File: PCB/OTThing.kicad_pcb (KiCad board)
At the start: 2 copper layers, 51.5 x 76.5 mm, 60 parts, among them IC1 TPS61041, J3 USB_C_Receptacle_USB2.0, Q1 BC858, Q2 BC847, Q3 BC847, Q4 BC858, Q5 BC858, Q6 BC847, Q7 BC858, SW1 RST/CONFIG, U1 ESP32-WROOM-32, U3 LTV-356T, U4 LTV-356T, U5 CH340C, U6 AMS1117-3.3

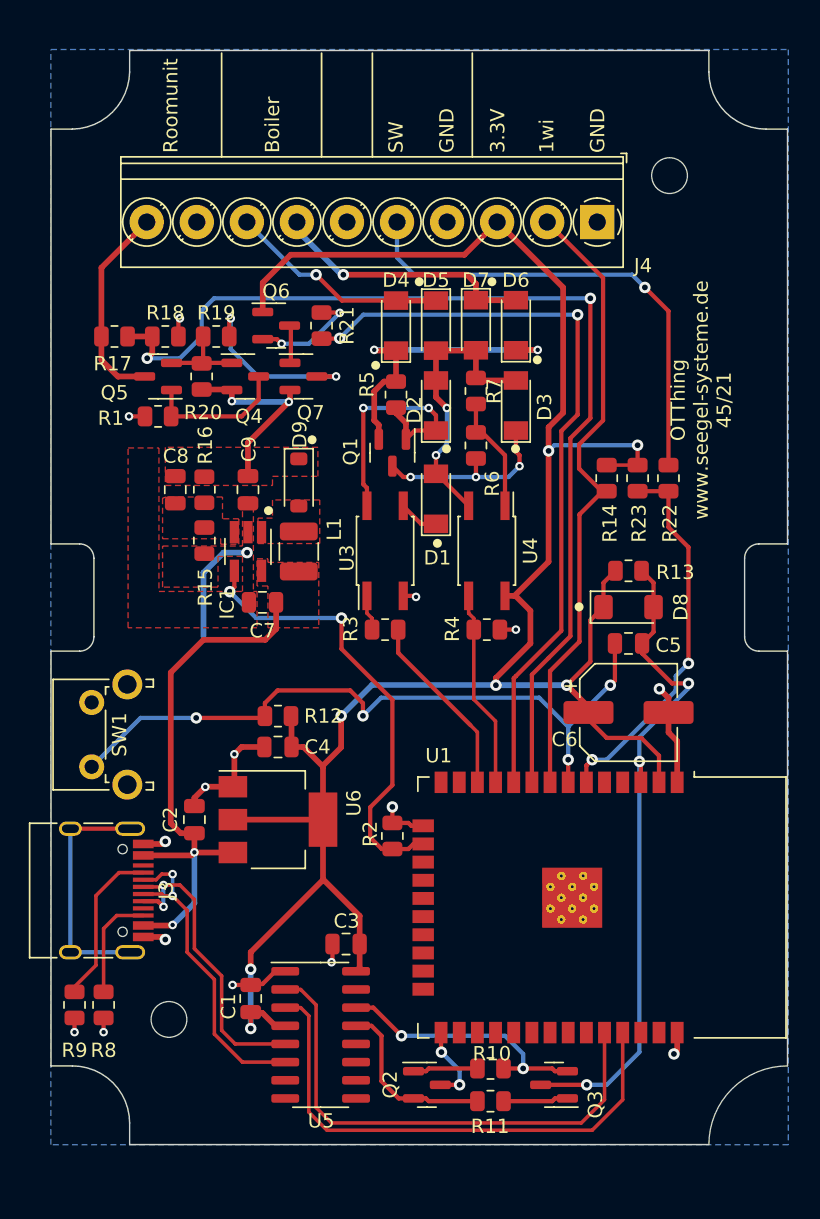
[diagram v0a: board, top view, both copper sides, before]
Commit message: change MCU redesign OT interfaces
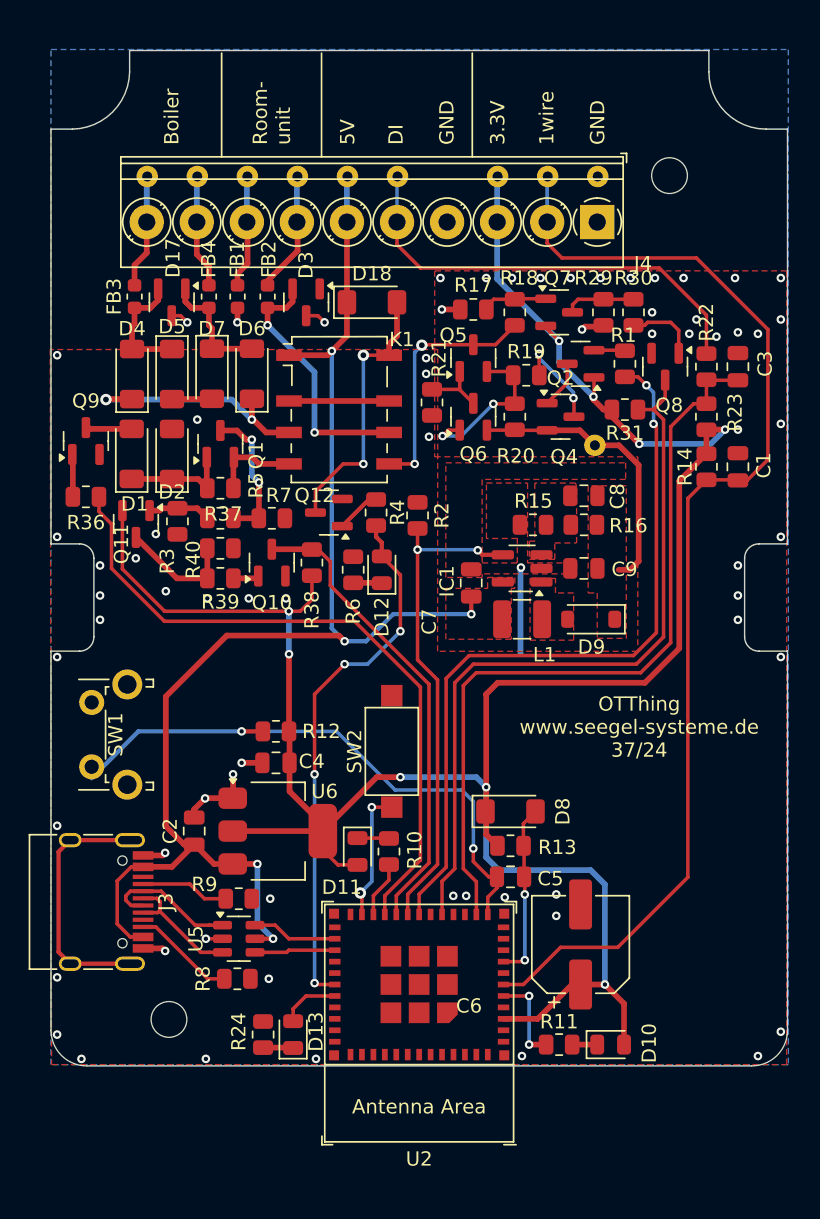
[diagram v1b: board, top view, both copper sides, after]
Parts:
- removed Q3: BC847, Package_TO_SOT_SMD:SOT-23
- removed U1: ESP32-WROOM-32, RF_Module:ESP32-WROOM-32
- removed U3, U4: LTV-356T, Package_SO:SO-4_4.4x3.6mm_P2.54mm
- added D10: RD, LED_SMD:LED_0805_2012Metric, F.Cu at (154.4, 143.9)
- added D11: GN, LED_SMD:LED_0805_2012Metric, F.Cu at (136.7, 130.4)
- added D12: YL, LED_SMD:LED_0805_2012Metric, F.Cu at (138.4, 110.7)
- added D13: GN, LED_SMD:LED_0805_2012Metric, F.Cu at (132.2, 143.2)
- added D17: D_Zener_Dual_CommonAnode_KKA_Parallel, Package_TO_SOT_SMD:SOT-23, F.Cu at (123.7, 92.0)
- added D18: LL4148, Diode_SMD:D_MiniMELF, F.Cu at (137.7, 92.0)
- added FB1: FerriteBead_Small, Inductor_SMD:L_0603_1608Metric, F.Cu at (128.3, 91.6)
- added FB2: FerriteBead_Small, Inductor_SMD:L_0603_1608Metric, F.Cu at (130.4, 91.6)
- added FB3: FerriteBead_Small, Inductor_SMD:L_0603_1608Metric, F.Cu at (121.1, 91.6)
- added FB4: FerriteBead_Small, Inductor_SMD:L_0603_1608Metric, F.Cu at (126.3, 91.6)
- added K1: G6K-2, Relay_SMD:Relay_DPDT_Omron_G6K-2F-Y, F.Cu at (135.4, 99.5)
- added Q10: BC847C, Package_TO_SOT_SMD:SOT-23, F.Cu at (130.7, 110.2)
- added Q11: BC857C, Package_TO_SOT_SMD:SOT-23, F.Cu at (121.2, 107.5)
- added Q12: BC847C, Package_TO_SOT_SMD:SOT-23, F.Cu at (134.7, 106.7)
- added Q8: BC847C, Package_TO_SOT_SMD:SOT-23, F.Cu at (158.2, 96.5)
- added Q9: BC847C, Package_TO_SOT_SMD:SOT-23, F.Cu at (117.7, 101.7)
- added R24: 100, Resistor_SMD:R_0805_2012Metric, F.Cu at (130.1, 143.2)
- added R29: 4k7, Resistor_SMD:R_0805_2012Metric, F.Cu at (153.9, 92.7)
- added R30: 4k7, Resistor_SMD:R_0805_2012Metric, F.Cu at (156.0, 92.7)
- added R31: 4k7, Resistor_SMD:R_0805_2012Metric, F.Cu at (155.4, 99.5)
- added R36: 4k7, Resistor_SMD:R_0805_2012Metric, F.Cu at (117.7, 105.6)
- added R37: 10k, Resistor_SMD:R_0805_2012Metric, F.Cu at (127.1, 107.1)
- added R38: 4k7, Resistor_SMD:R_0805_2012Metric, F.Cu at (133.5, 110.2)
- added R39: 4k7, Resistor_SMD:R_0805_2012Metric, F.Cu at (127.1, 111.3)
- added R40: 4k7, Resistor_SMD:R_0805_2012Metric, F.Cu at (127.1, 109.2)
- added SW2: BOOT, Button_Switch_SMD:SW_SPST_CK_RS282G05A3, F.Cu at (139.1, 123.4)
- added TP1: ~, TestPoint:TestPoint_THTPad_D1.5mm_Drill0.7mm, B.Cu at (153.5, 83.2)
- added TP10: ~, TestPoint:TestPoint_THTPad_D1.5mm_Drill0.7mm, B.Cu at (153.3, 102.0)
- added TP2: ~, TestPoint:TestPoint_THTPad_D1.5mm_Drill0.7mm, B.Cu at (150.0, 83.2)
- added TP3: ~, TestPoint:TestPoint_THTPad_D1.5mm_Drill0.7mm, B.Cu at (146.5, 83.2)
- added TP4: ~, TestPoint:TestPoint_THTPad_D1.5mm_Drill0.7mm, B.Cu at (139.5, 83.2)
- added TP5: ~, TestPoint:TestPoint_THTPad_D1.5mm_Drill0.7mm, B.Cu at (136.0, 83.2)
- added TP6: ~, TestPoint:TestPoint_THTPad_D1.5mm_Drill0.7mm, B.Cu at (132.5, 83.2)
- added TP7: ~, TestPoint:TestPoint_THTPad_D1.5mm_Drill0.7mm, B.Cu at (129.0, 83.2)
- added TP8: ~, TestPoint:TestPoint_THTPad_D1.5mm_Drill0.7mm, B.Cu at (125.5, 83.2)
- added TP9: ~, TestPoint:TestPoint_THTPad_D1.5mm_Drill0.7mm, B.Cu at (122.0, 83.2)
- added U2: ESP32-C3-MINI-1, User:ESP32-C3-MINI-1, F.Cu at (141.0, 142.4)
- C1, C3: value 100n -> 470pF
- D1: value TZMC4V3 -> ZMM4V3
- D3: value ZMM4,7 -> D_Zener_Dual_CommonAnode_KKA_Parallel; footprint Diode_SMD:D_MiniMELF -> Package_TO_SOT_SMD:SOT-23
- D9: value MBR0530 -> MBR0540
- Q1, Q4, Q5, Q7: value BC858 -> BC857C
- Q2: value BC847 -> BC847C
- Q6: value BC847 -> BC857C
- R1: value 33k -> 4k7
- R10, R11: value 3k3 -> 100
- R17: value 33k -> 6k8
- R18: value 3k3 -> 22k
- R21: value 3k3 -> 33k
- R3: value 330 -> 18k
- R4: value 1k5 -> 4k7
- R5: value 330 -> 470
- R6: value 220 -> 100
- R7: value 100 -> 330
- U5: value CH340C -> USBLC6-2SC6; footprint Package_SO:SOIC-16_3.9x9.9mm_P1.27mm -> Package_TO_SOT_SMD:SOT-23-6
- moved Q2 51.5 mm to (152.3, 96.3), turned to 180 degrees
- moved C1 50.4 mm to (163.3, 103.5), turned to 90 degrees
- moved C3 48.8 mm to (163.3, 96.5), turned to 90 degrees
- moved R1 32.8 mm to (155.4, 96.3), turned to -90 degrees
- moved C8 28.6 mm to (152.6, 105.5), turned to 180 degrees
- moved R16 26.6 mm to (152.6, 107.6), turned to 180 degrees
- moved R17 25.2 mm to (144.8, 92.5)
- moved R18 24.5 mm to (147.7, 92.7), turned to -90 degrees
- moved C9 24.1 mm to (152.6, 110.6), turned to 180 degrees
- moved R15 23.0 mm to (149.0, 107.6), turned to 180 degrees
- moved D9 22.6 mm to (153.1, 114.2), turned to 180 degrees
- moved R2 22.5 mm to (140.9, 106.9)
- moved Q4 22.2 mm to (150.9, 100.0)
- moved Q5 22.1 mm to (144.8, 95.9), turned to 90 degrees
- moved R20 22.1 mm to (147.7, 100.0)
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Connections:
- net /BTN renamed /CFG
- net /RST renamed /EN
- C1 pad 1: GND -> /DQ
- C1 pad 2: +3.3V -> GND
- C3 pad 1: +3.3V -> Net-(U2-GPIO1/ADC1_CH1/XTAL_32K_N)
- D2 pad 1: Net-(D2-K) -> Net-(D1-K)
- D2 pad 2: Net-(D1-A) -> GND
- D3 pad 1: Net-(D3-K) -> unconnected-(D3-K-Pad1)
- D3 pad 2: Net-(D1-A) -> Net-(D3-K-Pad2)
- D5 pad 2: Net-(D1-A) -> GND
- D7 pad 2: Net-(D1-A) -> GND
- J3 pad A6: Net-(U5-UD+) -> Net-(J3-D+-PadA6)
- J3 pad A7: Net-(U5-UD-) -> Net-(J3-D--PadA7)
- J3 pad B6: Net-(U5-UD+) -> Net-(J3-D+-PadA6)
- J3 pad B7: Net-(U5-UD-) -> Net-(J3-D--PadA7)
- J4 pad 10: Net-(J4-Pin_10) -> /OpenTherm interface/OTMASTER_A
- J4 pad 6: unconnected-(J4-Pin_6-Pad6) -> +5V
- J4 pad 7: Net-(D6-A) -> /OpenTherm interface/OTSLAVE_B
- J4 pad 8: Net-(D4-A) -> /OpenTherm interface/OTSLAVE_A
- J4 pad 9: GND -> /OpenTherm interface/OTMASTER_B
- Q1 pad 1: Net-(D2-K) -> Net-(D1-K)
- Q1 pad 2: Net-(D4-K) -> Net-(Q1-E)
- Q1 pad 3: Net-(D3-K) -> Net-(Q1-C)
- Q2 pad 1: Net-(Q2-B) -> +3.3V
- Q2 pad 3: /GP0 -> Net-(Q2-C)
- Q4 pad 1: Net-(Q4-B) -> Net-(Q2-C)
- Q5 pad 1: Net-(Q4-C) -> Net-(Q5-B)
- Q5 pad 2: Net-(Q4-B) -> Net-(Q5-E)
- Q5 pad 3: Net-(J4-Pin_10) -> Net-(Q5-C)
- Q6 pad 1: +3.3V -> Net-(Q5-E)
- Q6 pad 2: Net-(Q6-E) -> +24V
- Q6 pad 3: Net-(Q6-C) -> Net-(Q5-B)
- Q7 pad 1: Net-(Q6-C) -> Net-(Q7-B)
- Q7 pad 2: +24V -> +3.3V
- R1 pad 1: GND -> Net-(Q2-E)
- R1 pad 2: Net-(Q4-C) -> /OTS_TX
- R10 pad 1: Net-(Q3-E) -> Net-(U2-GPIO8)
- R10 pad 2: Net-(Q2-B) -> Net-(D11-K)
- R11 pad 1: Net-(Q2-E) -> Net-(U2-GPIO2/ADC1_CH2)
- R17 pad 1: /OTS_IN -> Net-(Q7-B)
- R17 pad 2: Net-(J4-Pin_10) -> GND
- R18 pad 1: /OTS_IN -> Net-(Q7-B)
- R18 pad 2: GND -> Net-(Q5-C)
- R19 pad 1: Net-(Q4-B) -> Net-(Q5-E)
- R19 pad 2: Net-(Q7-C) -> Net-(Q4-C)
- R20 pad 1: Net-(Q4-B) -> Net-(Q5-E)
- R21 pad 1: Net-(Q6-E) -> GND
- R21 pad 2: /OTS_OUT -> Net-(Q5-B)
- R22 pad 2: Net-(U1-IO34) -> Net-(U2-GPIO1/ADC1_CH1/XTAL_32K_N)
- R23 pad 1: Net-(U1-IO34) -> Net-(U2-GPIO1/ADC1_CH1/XTAL_32K_N)
- R3 pad 1: Net-(R3-Pad1) -> GND
- R3 pad 2: /OTM_OUT -> Net-(Q11-B)
- R4 pad 1: GND -> Net-(Q12-B)
- R4 pad 2: /OTM_IN -> /REL
- R5 pad 1: Net-(D4-K) -> Net-(Q1-E)
- R5 pad 2: Net-(D2-K) -> Net-(D1-K)
- R6 pad 1: Net-(D3-K) -> GND
- R6 pad 2: Net-(R6-Pad2) -> Net-(D12-K)
- R7 pad 1: Net-(R6-Pad2) -> Net-(Q1-C)
- R7 pad 2: Net-(D1-A) -> GND
- U5 pad 1: GND -> Net-(J3-D--PadA7)
- U5 pad 2: /RXD -> GND
- U5 pad 3: /TXD -> Net-(J3-D+-PadA6)
- U5 pad 4: +3.3V -> /DP
- U5 pad 5: Net-(U5-UD+) -> +5V
- U5 pad 6: Net-(U5-UD-) -> /DM
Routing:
- net /OTS_IN: track 72.7 -> 0.00 mm, vias 2 -> 0
- net +5V: track 38.9 -> 96.9 mm, vias 2 -> 5
- net Net-(U2-GPIO1/ADC1_CH1/XTAL_32K_N): track 0.00 -> 54.3 mm
- net /OTS_OUT: track 53.1 -> 0.00 mm, vias 2 -> 0
- net /OTS_TX: track 0.00 -> 52.6 mm, vias 0 -> 2
- net /OTS_RX: track 0.00 -> 52.2 mm
- net /OTM_TX: track 0.00 -> 47.3 mm
- net /REL: track 0.00 -> 37.6 mm, vias 0 -> 4
- net /TXD: track 36.7 -> 0.00 mm
- net /DQ: track 44.3 -> 81.0 mm
- net /RXD: track 35.8 -> 0.00 mm
- net /EN: track 47.1 -> 11.9 mm, vias 3 -> 2
- net /OTM_RX: track 0.00 -> 32.9 mm
- net Net-(U1-IO34): track 26.6 -> 0.00 mm, vias 2 -> 0
- net Net-(U5-UD-): track 22.5 -> 0.00 mm, vias 2 -> 0
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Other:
- board size 51.5 x 76.5 mm -> 51.5 x 71 mm
- board text added: "1wire"
- board text added: "5V"
- board text added: "DI"
- board text added: "OTThing www.seegel-systeme.de 37/24"
- board text added: "Room- unit"
- board text removed: "1wi"
- board text removed: "OTThing www.seegel-systeme.de 45/21"
- board text removed: "Roomunit"
- board text removed: "SW"

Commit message: Change MCU
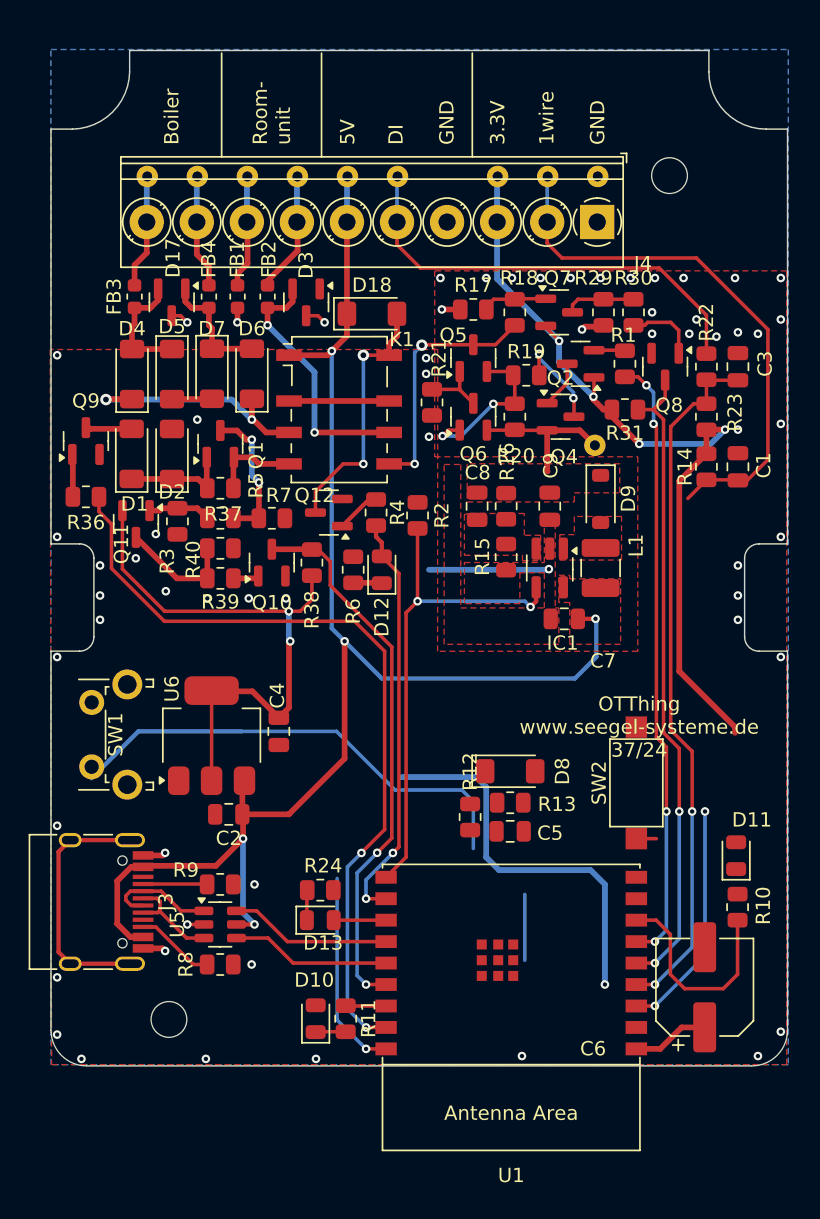
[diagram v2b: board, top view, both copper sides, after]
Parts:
- removed U2: ESP32-C3-MINI-1, User:ESP32-C3-MINI-1
- added U1: ESP32-C3-WROOM-02, User:ESP32-C3-WROOM-02, F.Cu at (147.5, 138.3)
- moved D11 26.5 mm to (163.2, 130.7), turned to 90 degrees
- moved R10 24.7 mm to (163.3, 134.3)
- moved D10 20.7 mm to (133.8, 142.1), turned to 90 degrees
- moved SW2 17.2 mm to (156.2, 125.6)
- moved R11 15.0 mm to (135.9, 142.1), turned to -90 degrees
- moved R12 14.8 mm to (144.6, 128.0), turned to 90 degrees
- moved R24 10.9 mm to (134.1, 133.1), turned to 180 degrees
- moved C6 9.18 mm to (161.0, 139.9)
- moved D9 8.44 mm to (153.7, 105.8), turned to -90 degrees
- moved D13 8.22 mm to (134.1, 135.2), turned to 0 degrees
- moved U6 8.12 mm to (126.5, 122.3), turned to 90 degrees
- moved C8 7.50 mm to (145.1, 106.3), turned to -90 degrees
- moved C7 6.97 mm to (151.2, 114.1), turned to 180 degrees
- moved L1 6.56 mm to (153.7, 110.6), turned to 90 degrees
- moved R16 5.59 mm to (147.1, 106.3), turned to -90 degrees
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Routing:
- net +3.3V: track 172.2 -> 130.6 mm, vias 9 -> 7
- net /DQ: track 81.0 -> 54.8 mm, vias 0 -> 2
- net Net-(U1-GPIO8): track 3.94 -> 14.8 mm
- net /OTS_TX: track 52.6 -> 42.9 mm, vias 2 -> 4
- net +24V: track 20.0 -> 10.9 mm
- net /OTM_TX: track 47.3 -> 56.2 mm, vias 0 -> 2
- net /REL: track 37.6 -> 29.1 mm, vias 4 -> 2
- net Net-(U1-GPIO9): track 9.28 -> 1.40 mm, vias 2 -> 0
- net /EN: track 11.9 -> 4.60 mm, vias 2 -> 0
- net /OTS_RX: track 52.2 -> 44.9 mm, vias 0 -> 2
- net /CFG: track 40.8 -> 47.5 mm, vias 2 -> 1
- net +5V: track 96.9 -> 103.6 mm
- net /DP: track 5.64 -> 11.2 mm
- net /OTM_RX: track 32.9 -> 38.5 mm, vias 0 -> 2
- net /DM: track 5.97 -> 11.4 mm
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
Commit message: finish 45/24
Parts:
- K1: value G6K-2 -> G6K-2F-Y-5V
- moved D10 12.8 mm to (133.4, 129.3)
- moved R11 9.52 mm to (133.4, 132.9), turned to 90 degrees
- moved D13 5.97 mm to (135.5, 129.4), turned to -90 degrees
- moved R24 1.41 mm to (135.5, 132.9), turned to -90 degrees
- moved D11 0.12 mm to (163.3, 130.7)
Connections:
- D13 pad 1: Net-(D13-K) -> GND
- R24 pad 1: GND -> Net-(D13-A)
- R24 pad 2: Net-(D13-K) -> Net-(U1-GPIO21/U0TXD)
- U1 pad 12: Net-(D13-A) -> Net-(U1-GPIO21/U0TXD)
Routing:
- net +3.3V: track 130.6 -> 182.0 mm, vias 7 -> 8
- net /DQ: track 54.8 -> 77.2 mm
- net /EN: track 4.60 -> 26.4 mm, vias 0 -> 2
- net Net-(U1-GPIO2/ADC1_CH2): track 2.83 -> 11.8 mm, vias 0 -> 2
- net Net-(U1-GPIO9): track 1.40 -> 8.00 mm
- net Net-(U1-GPIO21/U0TXD): track 0.00 -> 4.15 mm
- net /CFG: track 47.5 -> 49.7 mm, vias 1 -> 2
- net Net-(D13-K): track 2.11 -> 0.00 mm
- net Net-(D13-A): track 3.66 -> 1.75 mm
- net Net-(D11-K): track 0.00 -> 1.76 mm
- net +5V: track 103.6 -> 102.7 mm
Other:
- board text added: "Boot"
- board text added: "OTThing www.seegel-systeme.de 45/24"
- board text added: "Reset/Config"
- board text removed: "OTThing www.seegel-systeme.de 37/24"

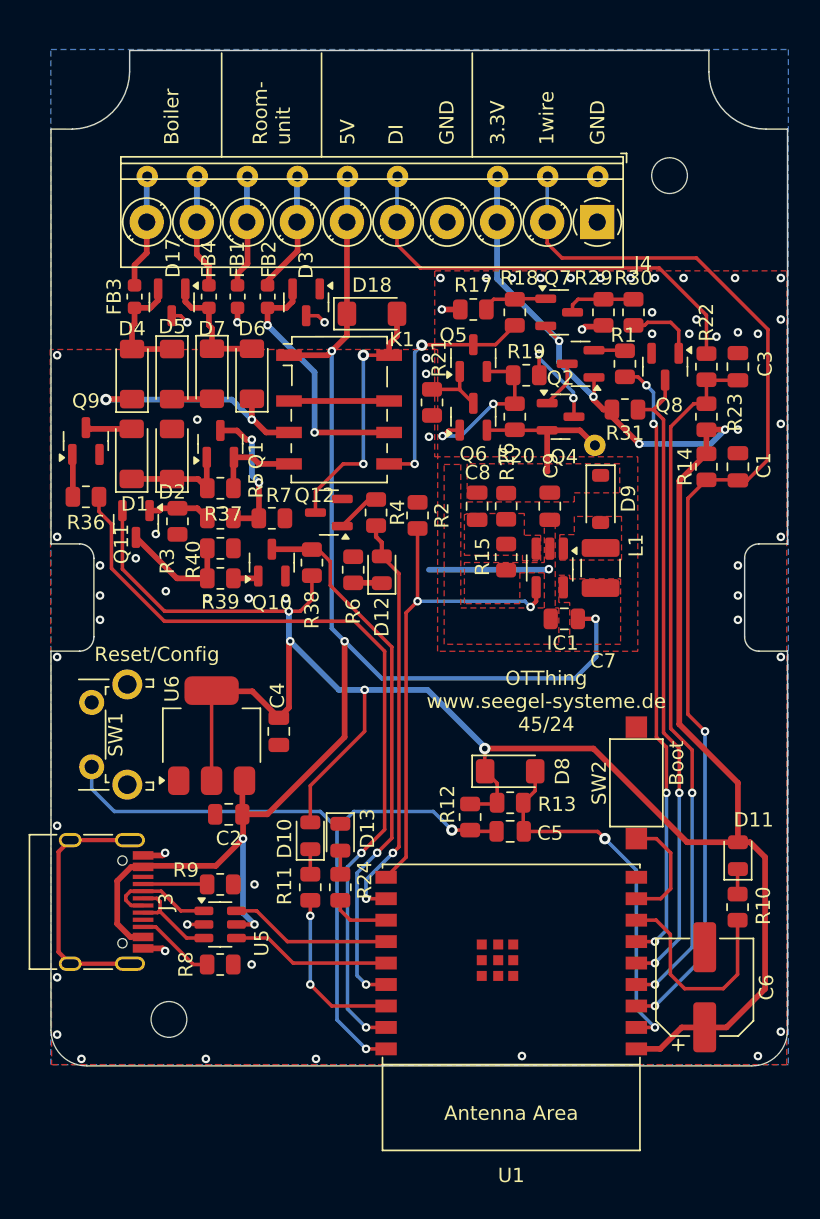
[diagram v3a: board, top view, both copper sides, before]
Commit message: add pullups for stability
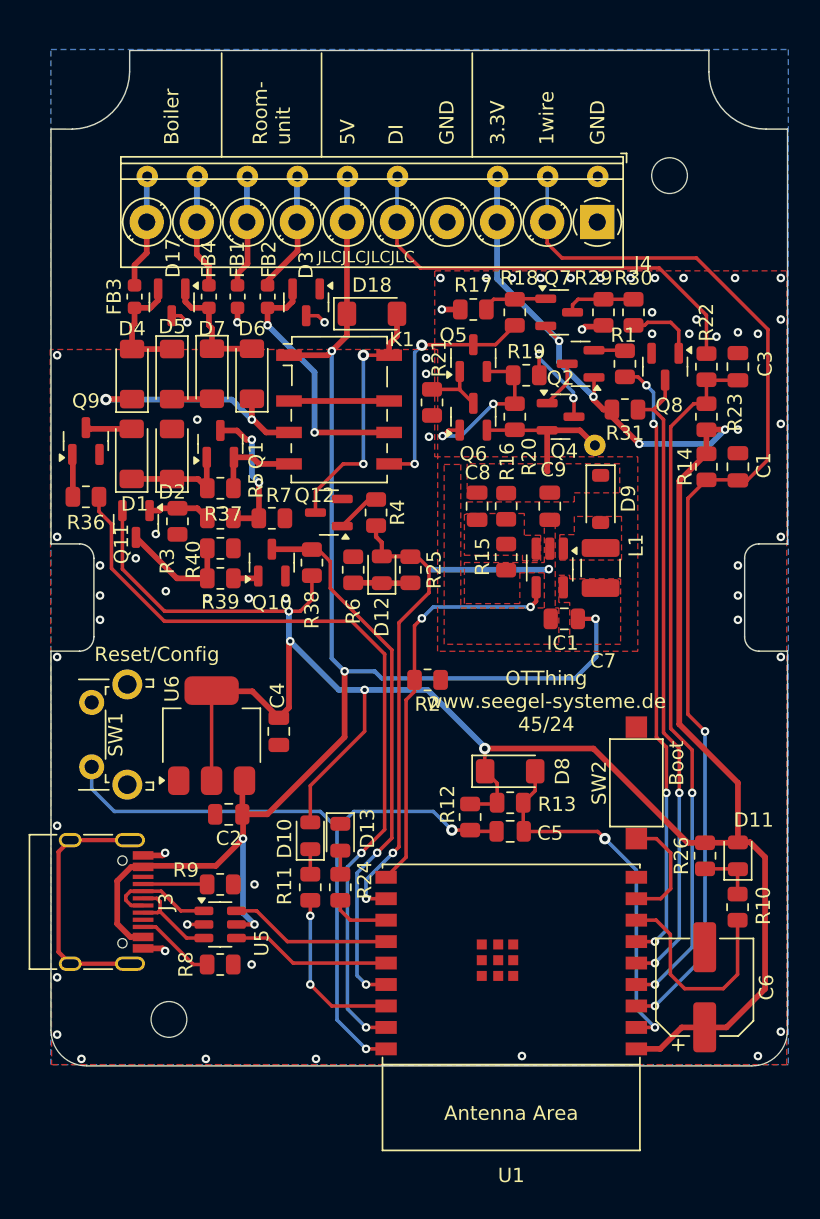
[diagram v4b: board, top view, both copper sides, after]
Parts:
- added R25: 12k, Resistor_SMD:R_0805_2012Metric, F.Cu at (140.4, 110.7)
- added R26: 12k, Resistor_SMD:R_0805_2012Metric, F.Cu at (161.0, 130.7)
- moved R2 11.5 mm to (141.6, 118.4), turned to 180 degrees
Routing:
- net /EN24: track 34.9 -> 28.6 mm
- net /REL: track 29.1 -> 32.3 mm
- net Net-(D11-K): track 1.76 -> 4.07 mm
- net Net-(D12-K): track 2.01 -> 4.02 mm
- net +5V: track 102.7 -> 101.8 mm
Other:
- board text added: "JLCJLCJLCJLC"
